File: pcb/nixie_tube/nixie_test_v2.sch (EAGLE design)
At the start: 21 parts, among them IC1 74141N

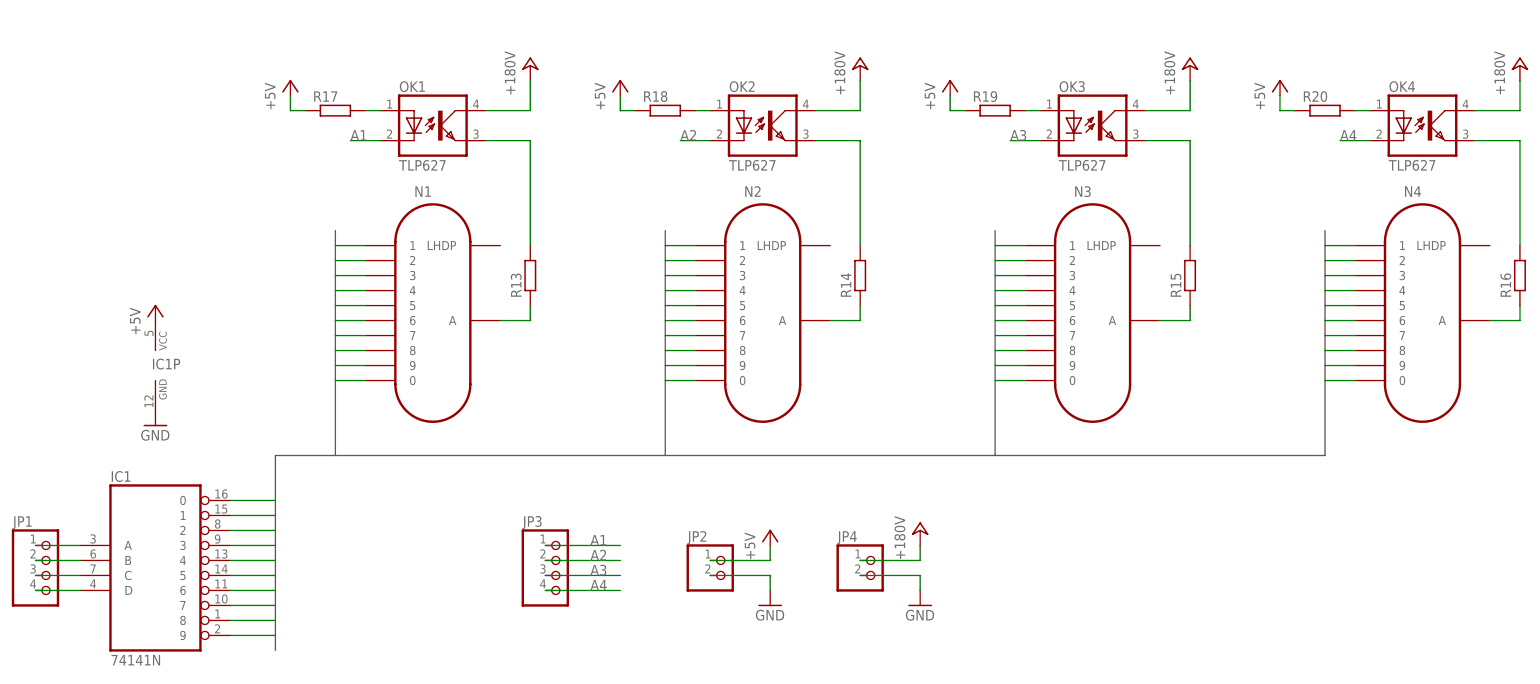
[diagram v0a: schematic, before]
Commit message: 
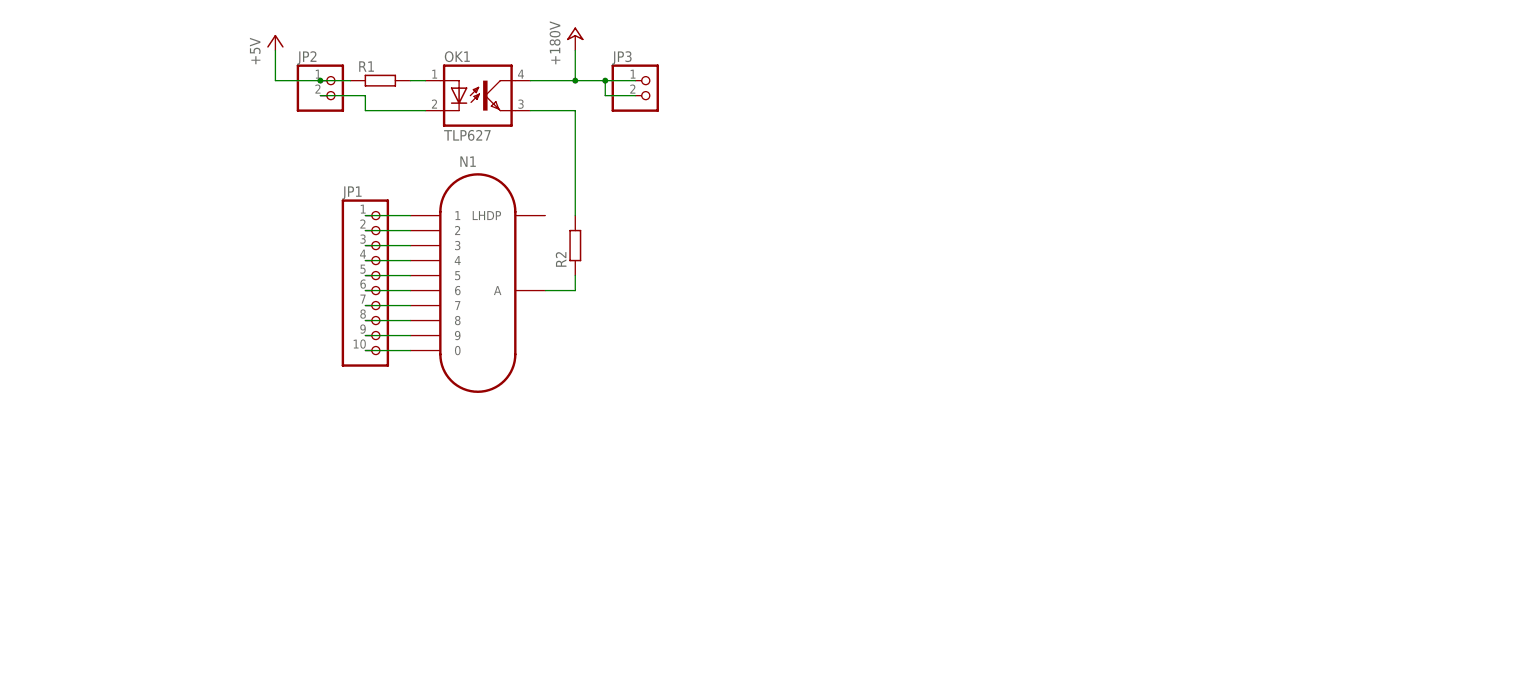
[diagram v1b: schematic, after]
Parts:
- removed IC1: 74141N, nixie_tube:74141N
- removed JP4: (no value), nixie_tube:PINHD-1X2
- removed N2, N3, N4: IN-12B, nixie_tube:IN-12B
- removed OK2, OK3, OK4: TLP627, nixie_tube:TLP627
- removed R13, R14, R15, R16, R17, R18, R19, R20: (no value), nixie_tube:R-EU_10
- added R1: (no value), nixie_tube:R-EU_R0805
- added R2: (no value), nixie_tube:R-EU_10
- JP1: device nixie_tube:PINHD-1X4 -> nixie_tube:PINHD-1X10
- JP3: device nixie_tube:PINHD-1X4 -> nixie_tube:PINHD-1X2
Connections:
- removed net A1: JP3.1, OK1.C
- removed net A2: JP3.2, OK2.C
- removed net A3: JP3.3, OK3.C
- removed net A4: JP3.4, OK4.C
- removed net GND: IC1P.GND, JP2.2, JP4.2
- removed net N$1: IC1A.A, JP1.1
- removed net N$13: N1.A, R13.1
- removed net N$14: OK1.EMIT, R13.2
- removed net N$15: N2.A, R14.1
- removed net N$16: OK2.EMIT, R14.2
- removed net N$19: N4.A, R16.1
- removed net N$20: OK4.EMIT, R16.2
- removed net N$21: OK1.A, R17.2
- removed net N$22: OK2.A, R18.2
- removed net N$24: OK4.A, R20.2
- removed net N$3: IC1A.C, JP1.3
- removed net N$4: IC1A.D, JP1.4
- net +24V: now also JP3.1, JP3.2; no longer JP4.1, OK2.COL, OK3.COL, OK4.COL
- net +5V: now also R1.1; no longer IC1P.VCC, R17.1, R18.1, R19.1, R20.1
- net C0: now also JP1.10; no longer IC1A.0, N2.0, N3.0, N4.0
- net C1: now also JP1.1; no longer IC1A.1, N2.1, N3.1, N4.1
- net C2: now also JP1.2; no longer IC1A.2, N2.2, N3.2, N4.2
- net C3: now also JP1.3; no longer IC1A.3, N2.3, N3.3, N4.3
- net C4: now also JP1.4; no longer IC1A.4, N2.4, N3.4, N4.4
- net C5: now also JP1.5; no longer IC1A.5, N2.5, N3.5, N4.5
- net C6: now also JP1.6; no longer IC1A.6, N2.6, N3.6, N4.6
- net C7: now also JP1.7; no longer IC1A.7, N2.7, N3.7, N4.7
- net C8: now also JP1.8; no longer IC1A.8, N2.8, N3.8, N4.8
- net C9: now also JP1.9; no longer IC1A.9, N2.9, N3.9, N4.9
- net N$17: now also N1.A, R2.1; no longer N3.A, R15.1
- net N$18: now also OK1.EMIT, R2.2; no longer OK3.EMIT, R15.2
- net N$2: now also JP2.2, OK1.C; no longer IC1A.B, JP1.2
- net N$23: now also OK1.A, R1.2; no longer OK3.A, R19.2
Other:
- moved on the sheet: JP2, N1, OK1
